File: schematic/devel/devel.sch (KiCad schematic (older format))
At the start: 61 parts, among them J1 CONN_PWR, J2 CONN_X1, J3 CONN_Y2, J4 CONN_X2, J5 CONN_Y1, U1 LM317_SOT223, U2 LM337_SOT223, U3 REF5010IDGK, U4 OPA4197

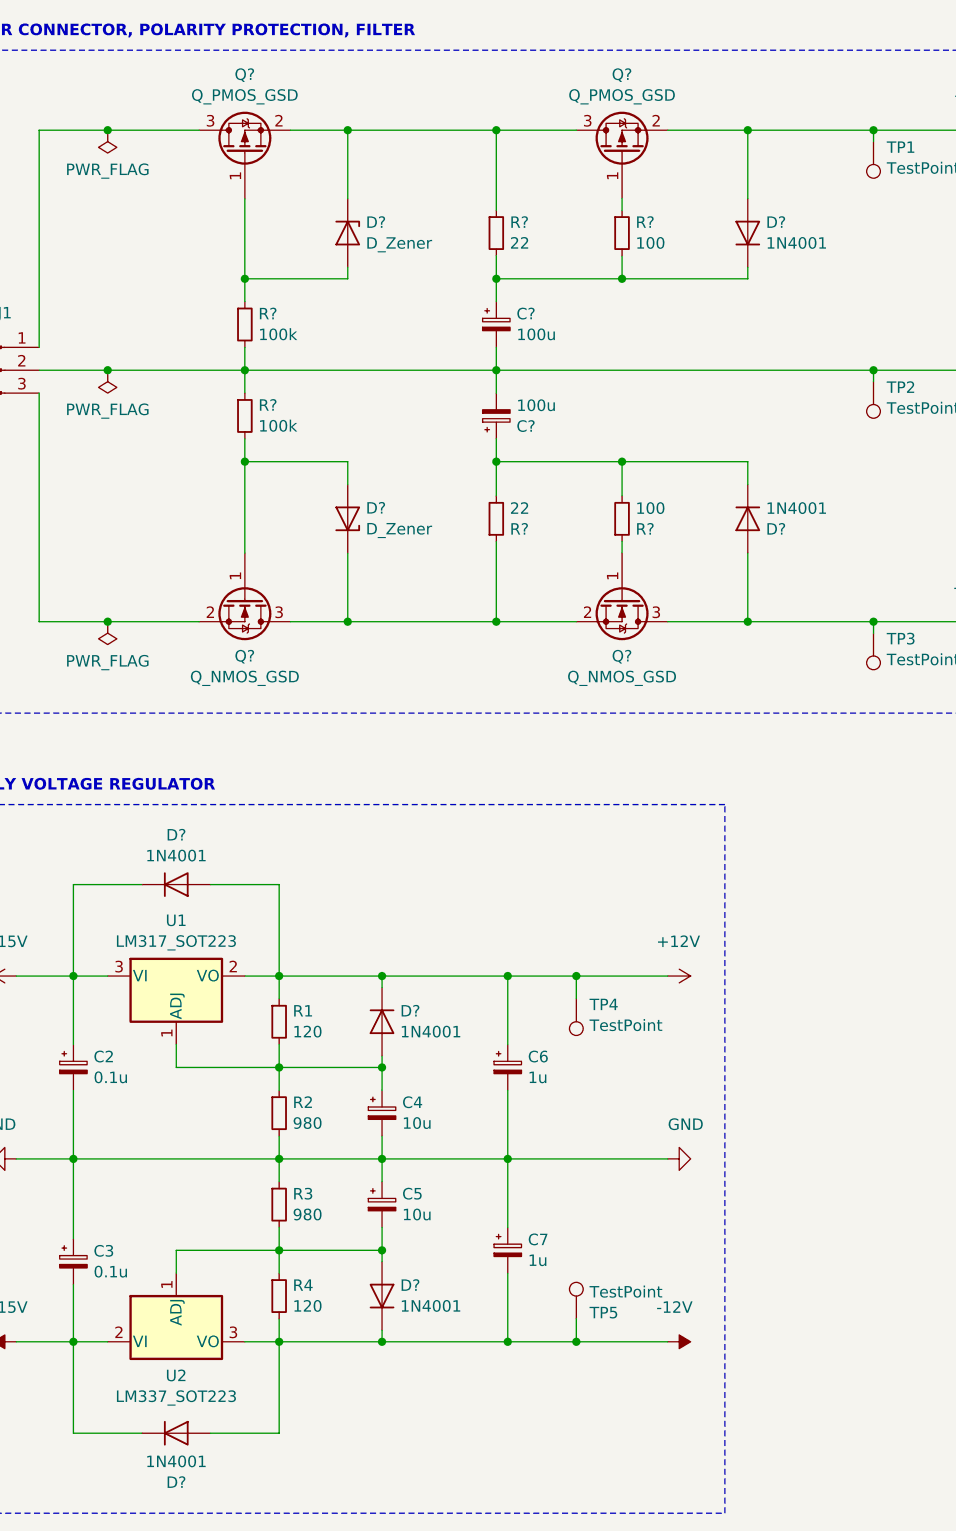
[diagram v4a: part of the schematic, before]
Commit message: updated footprint assignment
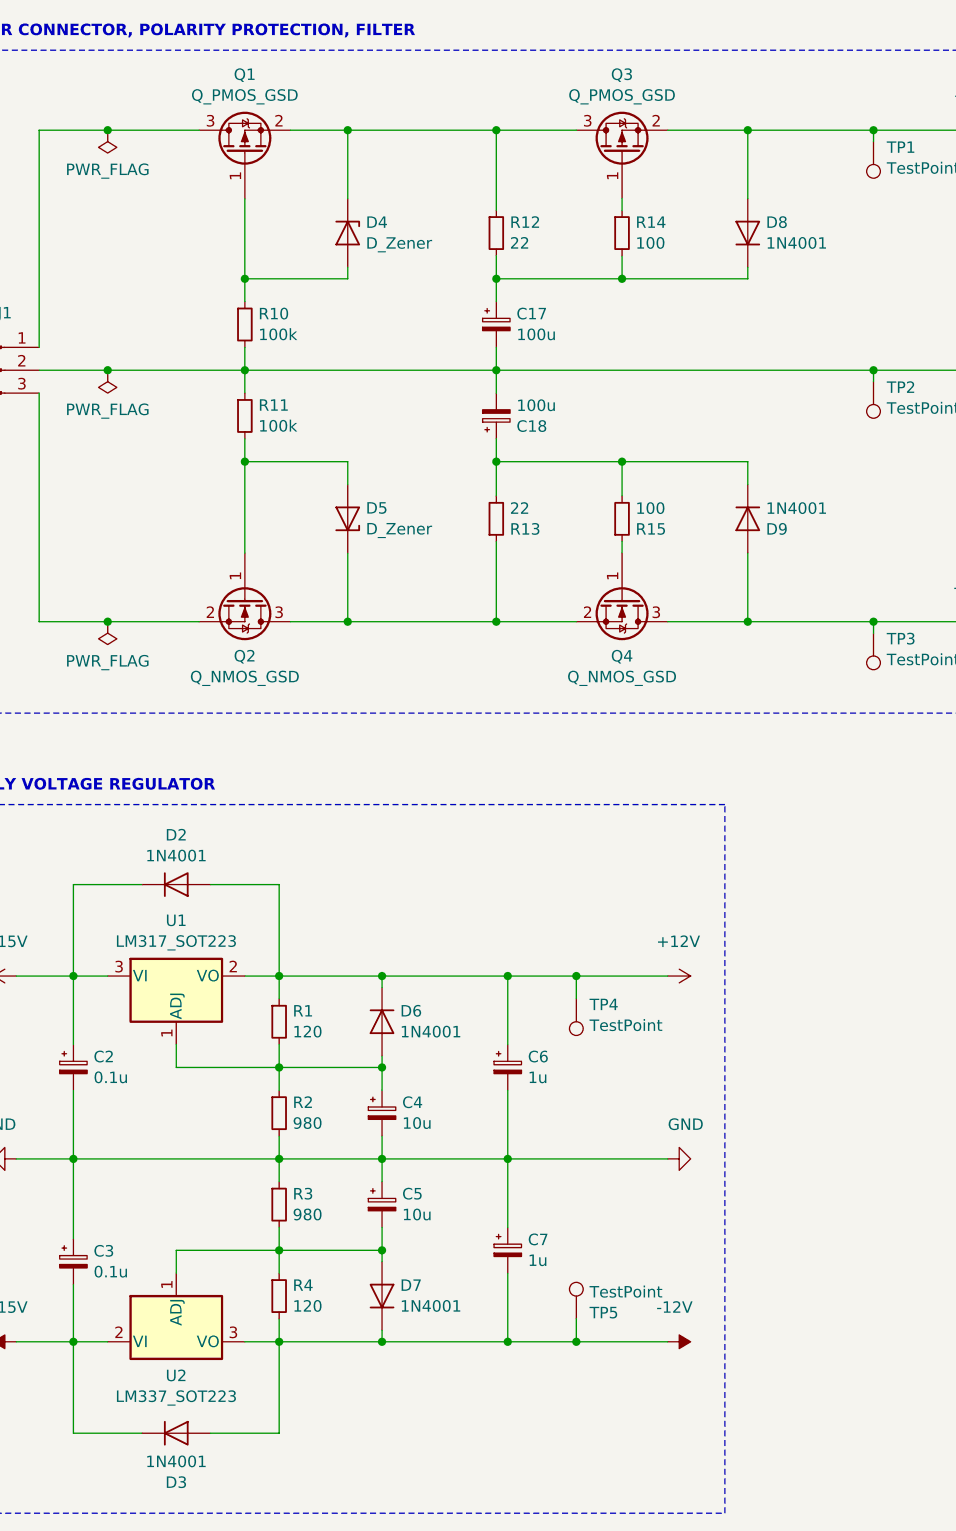
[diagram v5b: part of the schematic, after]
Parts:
- D4, D5: renamed from D?; footprint (none) -> Diode_SMD:D_0805_2012Metric
- Q1, Q2, Q3, Q4: renamed from Q?; footprint (none) -> Package_TO_SOT_SMD:SOT-23
- R10, R11, R12, R13, R14, R15: renamed from R?; footprint (none) -> Resistor_SMD:R_0805_2012Metric
- gave numbers to parts that had none: 8
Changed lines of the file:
@@
 	9300 5550 9300 5800
 $Comp
-L Device:Q_PMOS_GSD Q?
+L Device:Q_PMOS_GSD Q1
 U 1 1 5D363FE3
 P 1950 1200
-F 0 "Q?" V 2293 1200 50  0000 C CNN
+F 0 "Q1" V 2293 1200 50  0000 C CNN
 F 1 "Q_PMOS_GSD" V 2202 1200 50  0000 C CNN
-F 2 "" H 2150 1300 50  0001 C CNN
+F 2 "Package_TO_SOT_SMD:SOT-23" H 2150 1300 50  0001 C CNN
 F 3 "~" H 1950 1200 50  0001 C CNN
 	1    1950 1200
@@
 	1950 2150 3050 2150
 $Comp
-L Device:R_Small R?
+L Device:R_Small R10
 U 1 1 5D388B12
 P 1950 1950
-F 0 "R?" H 2009 1996 50  0000 L CNN
+F 0 "R10" H 2009 1996 50  0000 L CNN
 F 1 "100k" H 2009 1905 50  0000 L CNN
-F 2 "" H 1950 1950 50  0001 C CNN
+F 2 "Resistor_SMD:R_0805_2012Metric" H 1950 1950 50  0001 C CNN
 F 3 "~" H 1950 1950 50  0001 C CNN
 	1    1950 1950
@@
 Connection ~ 2400 1100
 $Comp
-L Device:Q_NMOS_GSD Q?
+L Device:Q_NMOS_GSD Q2
 U 1 1 5D3D4AC5
 P 1950 3150
-F 0 "Q?" V 2201 3150 50  0000 C CNN
+F 0 "Q2" V 2201 3150 50  0000 C CNN
 F 1 "Q_NMOS_GSD" V 2292 3150 50  0000 C CNN
-F 2 "" H 2150 3250 50  0001 C CNN
+F 2 "Package_TO_SOT_SMD:SOT-23" H 2150 3250 50  0001 C CNN
 F 3 "~" H 1950 3150 50  0001 C CNN
 	1    1950 3150
@@
 	1950 2950 1950 2550
 $Comp
-L Device:R_Small R?
+L Device:R_Small R11
 U 1 1 5D3EA970
 P 1950 2350
-F 0 "R?" H 2009 2396 50  0000 L CNN
+F 0 "R11" H 2009 2396 50  0000 L CNN
 F 1 "100k" H 2009 2305 50  0000 L CNN
-F 2 "" H 1950 2350 50  0001 C CNN
+F 2 "Resistor_SMD:R_0805_2012Metric" H 1950 2350 50  0001 C CNN
 F 3 "~" H 1950 2350 50  0001 C CNN
 	1    1950 2350
@@
 	650  7150 4050 7150
 $Comp
-L Diode:1N4001 D?
+L Diode:1N4001 D2
 U 1 1 5D4B45B0
 P 1650 4400
-F 0 "D?" H 1650 4184 50  0000 C CNN
+F 0 "D2" H 1650 4184 50  0000 C CNN
 F 1 "1N4001" H 1650 4275 50  0000 C CNN
 F 2 "Diode_THT:D_DO-41_SOD81_P10.16mm_Horizontal" H 1650 4225 50  0001 C CNN
@@
 	1800 4400 2100 4400
 $Comp
-L Diode:1N4001 D?
+L Diode:1N4001 D3
 U 1 1 5D4C0C3A
 P 1650 6800
-F 0 "D?" H 1650 6584 50  0000 C CNN
+F 0 "D3" H 1650 6584 50  0000 C CNN
 F 1 "1N4001" H 1650 6675 50  0000 C CNN
 F 2 "Diode_THT:D_DO-41_SOD81_P10.16mm_Horizontal" H 1650 6625 50  0001 C CNN
@@
 	2550 5300 2550 5200
 $Comp
-L Diode:1N4001 D?
+L Diode:1N4001 D6
 U 1 1 5D54EF79
 P 2550 5000
-F 0 "D?" V 2504 4921 50  0000 R CNN
+F 0 "D6" V 2504 4921 50  0000 R CNN
 F 1 "1N4001" V 2595 4921 50  0000 R CNN
 F 2 "Diode_THT:D_DO-41_SOD81_P10.16mm_Horizontal" H 2550 4825 50  0001 C CNN
@@
 	2550 4850 2550 4800
 $Comp
-L Diode:1N4001 D?
+L Diode:1N4001 D7
 U 1 1 5D54FA7D
 P 2550 6200
-F 0 "D?" V 2596 6279 50  0000 L CNN
+F 0 "D7" V 2596 6279 50  0000 L CNN
 F 1 "1N4001" V 2505 6279 50  0000 L CNN
 F 2 "Diode_THT:D_DO-41_SOD81_P10.16mm_Horizontal" H 2550 6025 50  0001 C CNN
@@
 	3050 1100 3400 1100
 $Comp
-L Device:R_Small R?
+L Device:R_Small R12
 U 1 1 5D5D52DE
 P 3050 1550
-F 0 "R?" H 3109 1596 50  0000 L CNN
+F 0 "R12" H 3109 1596 50  0000 L CNN
 F 1 "22" H 3109 1505 50  0000 L CNN
-F 2 "" H 3050 1550 50  0001 C CNN
+F 2 "Resistor_SMD:R_0805_2012Metric" H 3050 1550 50  0001 C CNN
 F 3 "~" H 3050 1550 50  0001 C CNN
 	1    3050 1550
@@
 	3050 1450 3050 1100
 $Comp
-L Device:Q_PMOS_GSD Q?
+L Device:Q_PMOS_GSD Q3
 U 1 1 5D5D688A
 P 3600 1200
-F 0 "Q?" V 3943 1200 50  0000 C CNN
+F 0 "Q3" V 3943 1200 50  0000 C CNN
 F 1 "Q_PMOS_GSD" V 3852 1200 50  0000 C CNN
-F 2 "" H 3800 1300 50  0001 C CNN
+F 2 "Package_TO_SOT_SMD:SOT-23" H 3800 1300 50  0001 C CNN
 F 3 "~" H 3600 1200 50  0001 C CNN
 	1    3600 1200
@@
 Connection ~ 3600 1750
 $Comp
-L Diode:1N4001 D?
+L Diode:1N4001 D8
 U 1 1 5D619651
 P 4150 1550
-F 0 "D?" V 4196 1471 50  0000 R CNN
+F 0 "D8" V 4196 1471 50  0000 R CNN
 F 1 "1N4001" V 4105 1471 50  0000 R CNN
 F 2 "Diode_THT:D_DO-41_SOD81_P10.16mm_Horizontal" H 4150 1375 50  0001 C CNN
@@
 	4150 1700 4150 1750
 $Comp
-L Device:R_Small R?
+L Device:R_Small R14
 U 1 1 5D63CFF8
 P 3600 1550
-F 0 "R?" H 3659 1596 50  0000 L CNN
+F 0 "R14" H 3659 1596 50  0000 L CNN
 F 1 "100" H 3659 1505 50  0000 L CNN
-F 2 "" H 3600 1550 50  0001 C CNN
+F 2 "Resistor_SMD:R_0805_2012Metric" H 3600 1550 50  0001 C CNN
 F 3 "~" H 3600 1550 50  0001 C CNN
 	1    3600 1550
@@
 	3050 2150 4700 2150
 $Comp
-L Device:R_Small R?
+L Device:R_Small R13
 U 1 1 5D6A3833
 P 3050 2800
-F 0 "R?" H 3109 2846 50  0000 L CNN
+F 0 "R13" H 3109 2846 50  0000 L CNN
 F 1 "22" H 3109 2755 50  0000 L CNN
-F 2 "" H 3050 2800 50  0001 C CNN
+F 2 "Resistor_SMD:R_0805_2012Metric" H 3050 2800 50  0001 C CNN
 F 3 "~" H 3050 2800 50  0001 C CNN
 	1    3050 2800
@@
 	3050 2900 3050 3250
 $Comp
-L Device:CP_Small C?
+L Device:CP_Small C18
 U 1 1 5D6A383A
 P 3050 2350
-AR Path="/5D6A383A" Ref="C?"  Part="1"
+AR Path="/5D6A383A" Ref="C18"  Part="1"
 AR Path="/5D7CE105/5D6A383A" Ref="C?"  Part="1"
-F 0 "C?" H 3138 2396 50  0000 L CNN
+F 0 "C18" H 3138 2396 50  0000 L CNN
 F 1 "100u" H 3138 2305 50  0000 L CNN
 F 2 "Capacitor_SMD:CP_Elec_4x3.9" H 3050 2350 50  0001 C CNN
@@
 Connection ~ 3600 2550
 $Comp
-L Diode:1N4001 D?
+L Diode:1N4001 D9
 U 1 1 5D6A3847
 P 4150 2800
-F 0 "D?" V 4196 2721 50  0000 R CNN
+F 0 "D9" V 4196 2721 50  0000 R CNN
 F 1 "1N4001" V 4105 2721 50  0000 R CNN
 F 2 "Diode_THT:D_DO-41_SOD81_P10.16mm_Horizontal" H 4150 2625 50  0001 C CNN
@@
 	4150 2650 4150 2550
 $Comp
-L Device:R_Small R?
+L Device:R_Small R15
 U 1 1 5D6A384E
 P 3600 2800
-F 0 "R?" H 3659 2846 50  0000 L CNN
+F 0 "R15" H 3659 2846 50  0000 L CNN
 F 1 "100" H 3659 2755 50  0000 L CNN
-F 2 "" H 3600 2800 50  0001 C CNN
+F 2 "Resistor_SMD:R_0805_2012Metric" H 3600 2800 50  0001 C CNN
 F 3 "~" H 3600 2800 50  0001 C CNN
 	1    3600 2800
@@
 	4150 3250 4700 3250
 $Comp
-L Device:Q_NMOS_GSD Q?
+L Device:Q_NMOS_GSD Q4
 U 1 1 5D6EB887
 P 3600 3150
-F 0 "Q?" V 3851 3150 50  0000 C CNN
+F 0 "Q4" V 3851 3150 50  0000 C CNN
 F 1 "Q_NMOS_GSD" V 3942 3150 50  0000 C CNN
-F 2 "" H 3800 3250 50  0001 C CNN
+F 2 "Package_TO_SOT_SMD:SOT-23" H 3800 3250 50  0001 C CNN
 F 3 "~" H 3600 3150 50  0001 C CNN
 	1    3600 3150
@@
 	3050 1850 3050 1750
 $Comp
-L Device:CP_Small C?
+L Device:CP_Small C17
 U 1 1 5D5D5F35
 P 3050 1950
-AR Path="/5D5D5F35" Ref="C?"  Part="1"
+AR Path="/5D5D5F35" Ref="C17"  Part="1"
 AR Path="/5D7CE105/5D5D5F35" Ref="C?"  Part="1"
-F 0 "C?" H 3138 1996 50  0000 L CNN
+F 0 "C17" H 3138 1996 50  0000 L CNN
 F 1 "100u" H 3138 1905 50  0000 L CNN
 F 2 "Capacitor_SMD:CP_Elec_4x3.9" H 3050 1950 50  0001 C CNN
@@
 $EndComp
 $Comp
-L Device:D_Zener D?
+L Device:D_Zener D4
 U 1 1 5D7A56EE
 P 2400 1550
-F 0 "D?" V 2354 1629 50  0000 L CNN
+F 0 "D4" V 2354 1629 50  0000 L CNN
 F 1 "D_Zener" V 2445 1629 50  0000 L CNN
-F 2 "" H 2400 1550 50  0001 C CNN
+F 2 "Diode_SMD:D_0805_2012Metric" H 2400 1550 50  0001 C CNN
 F 3 "~" H 2400 1550 50  0001 C CNN
 	1    2400 1550
@@
 $EndComp
 $Comp
-L Device:D_Zener D?
+L Device:D_Zener D5
 U 1 1 5D7A6478
 P 2400 2800
-F 0 "D?" V 2446 2879 50  0000 L CNN
+F 0 "D5" V 2446 2879 50  0000 L CNN
 F 1 "D_Zener" V 2355 2879 50  0000 L CNN
-F 2 "" H 2400 2800 50  0001 C CNN
+F 2 "Diode_SMD:D_0805_2012Metric" H 2400 2800 50  0001 C CNN
 F 3 "~" H 2400 2800 50  0001 C CNN
 	1    2400 2800

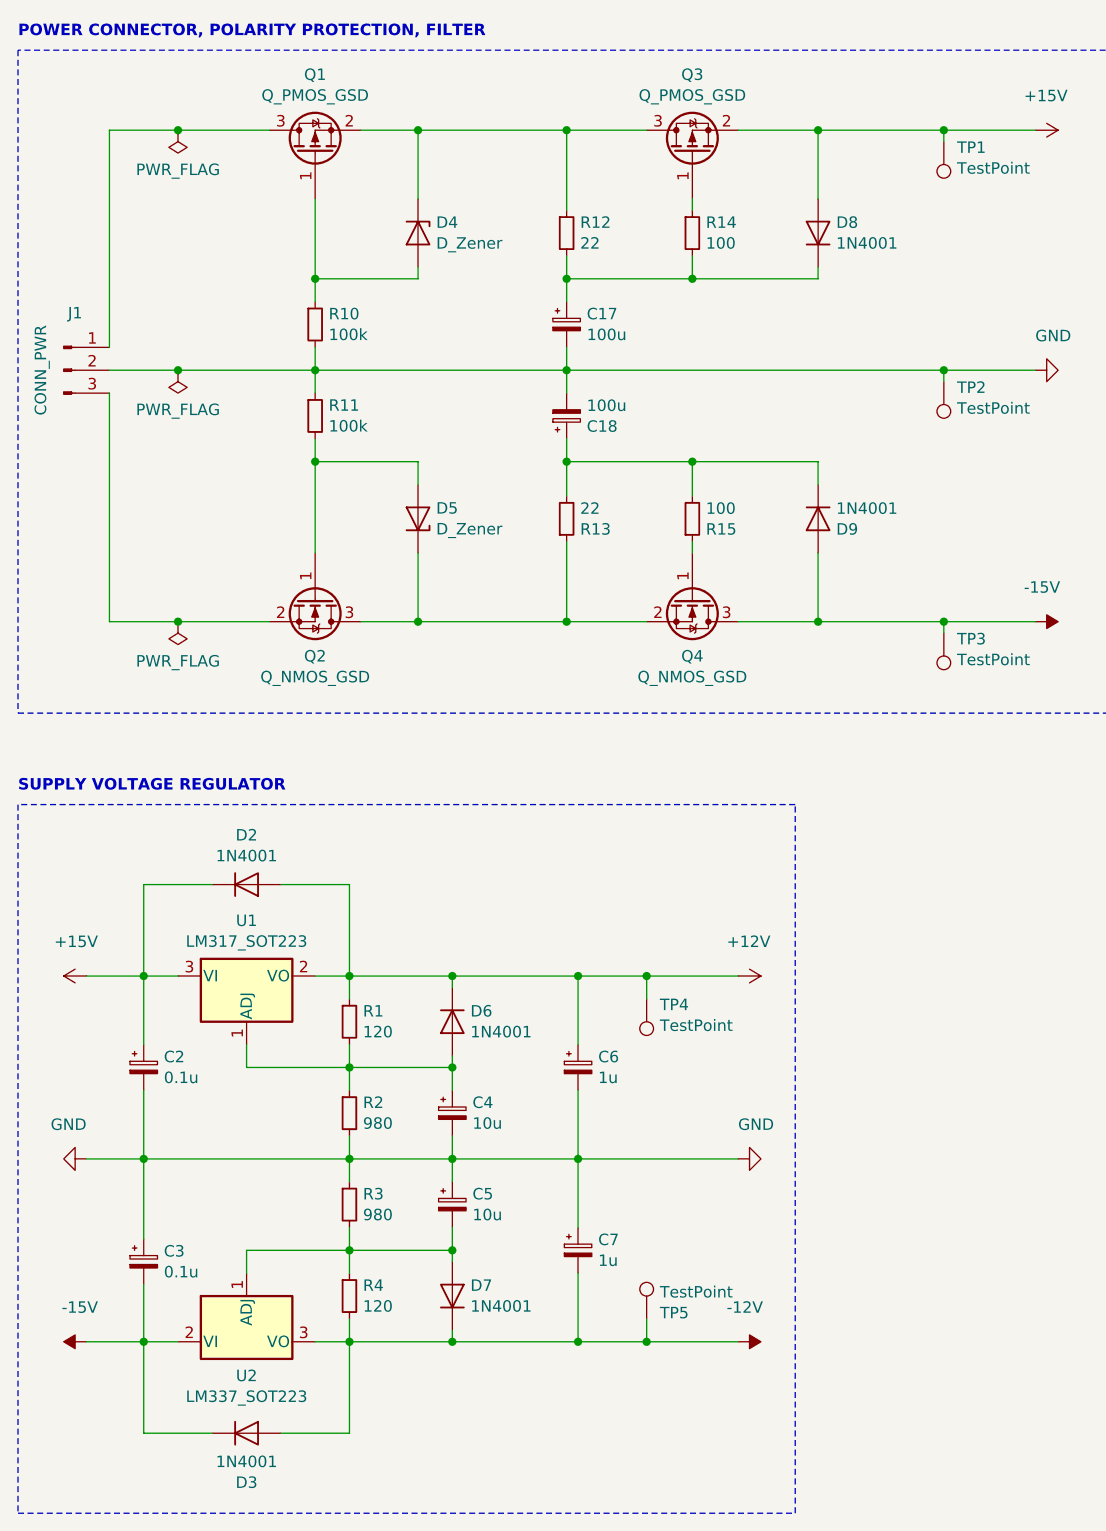
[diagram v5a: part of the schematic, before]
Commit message: changed diode circuit symbols to small, updated footprints
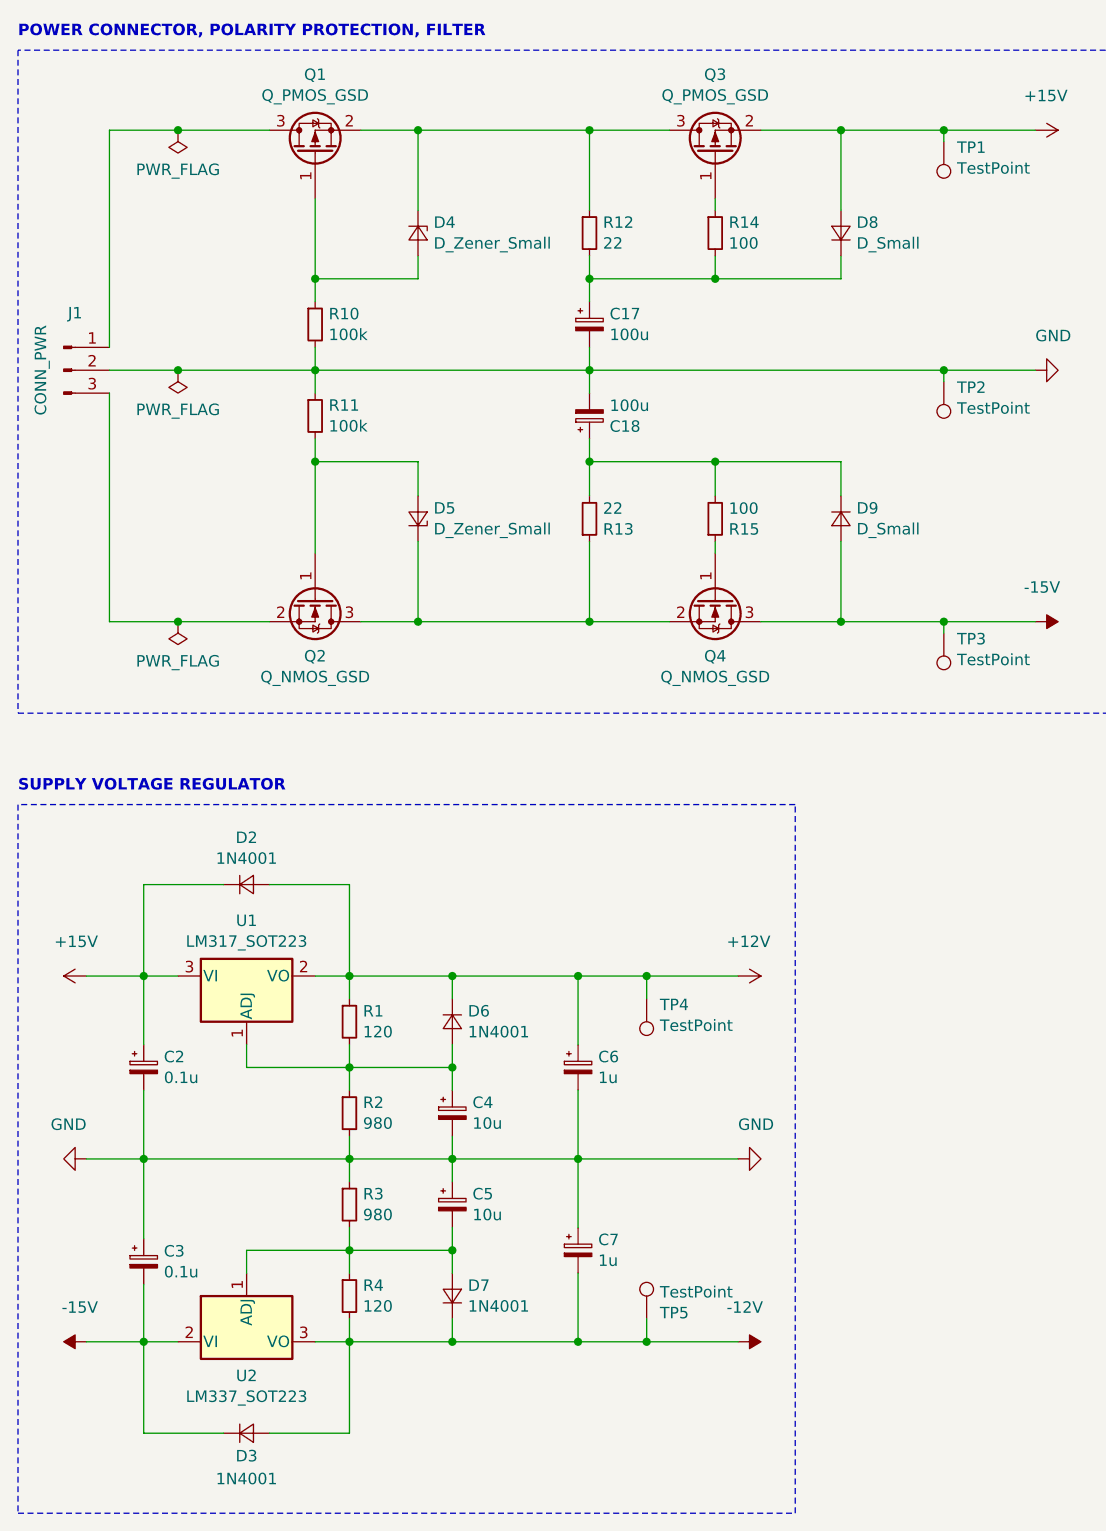
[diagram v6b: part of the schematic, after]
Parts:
- removed D2, D3, D6, D7, D8, D9: 1N4001, Diode_THT:D_DO-41_SOD81_P10.16mm_Horizontal, symbol Diode:1N4001
- removed D4, D5: D_Zener, Diode_SMD:D_0805_2012Metric, symbol Device:D_Zener
- added D2, D3, D6, D7: 1N4001, Diode_SMD:D_0805_2012Metric, symbol Device:D_Small
- added D4, D5: D_Zener_Small, Diode_SMD:D_0805_2012Metric, symbol Device:D_Zener_Small
- added D8, D9: D_Small, Diode_SMD:D_0805_2012Metric, symbol Device:D_Small
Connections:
- net +12V: now also D2.2 (A), D6.1 (K)
- net +15V: now also D2.1 (K), D8.2 (A)
- net -12V: now also D3.2 (A), D7.1 (K)
- net -15V: now also D3.1 (K), D9.2 (A)
- net at C5.2, R3.2, R4.1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: now also D7.2 (A)
- net at C4.1, R1.2, R2.1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: now also D6.2 (A)
- net at Q1.1 (G), R10.1: now also D4.2 (A)
- net at Q1.2 (S), Q3.3 (D), R12.1: now also D4.1 (K)
- net at Q2.1 (G), R11.2: now also D5.2 (A)
- net at Q2.3 (D), Q4.2 (S), R13.1: now also D5.1 (K)
- net at C17.1, R12.2, R14.2: now also D8.1 (K)
- net at C18.1, R13.2, R15.2: now also D9.1 (K)
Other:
- moved on the sheet: C17, C18, Q3, Q4, R12, R13, R14, R15
